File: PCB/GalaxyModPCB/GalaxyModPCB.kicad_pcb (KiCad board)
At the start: 2 copper layers, 63.5 x 38.2 mm, 65 parts, among them J1 LED RGBW Connector, J2 USB to UART, J3 Motor Connector, J4 Projector Connector, J5 Debug Header, J6 Power Header, J7 Boot mode, Q1 IRLML0030, Q2 IRLML0030, Q3 IRLML0030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

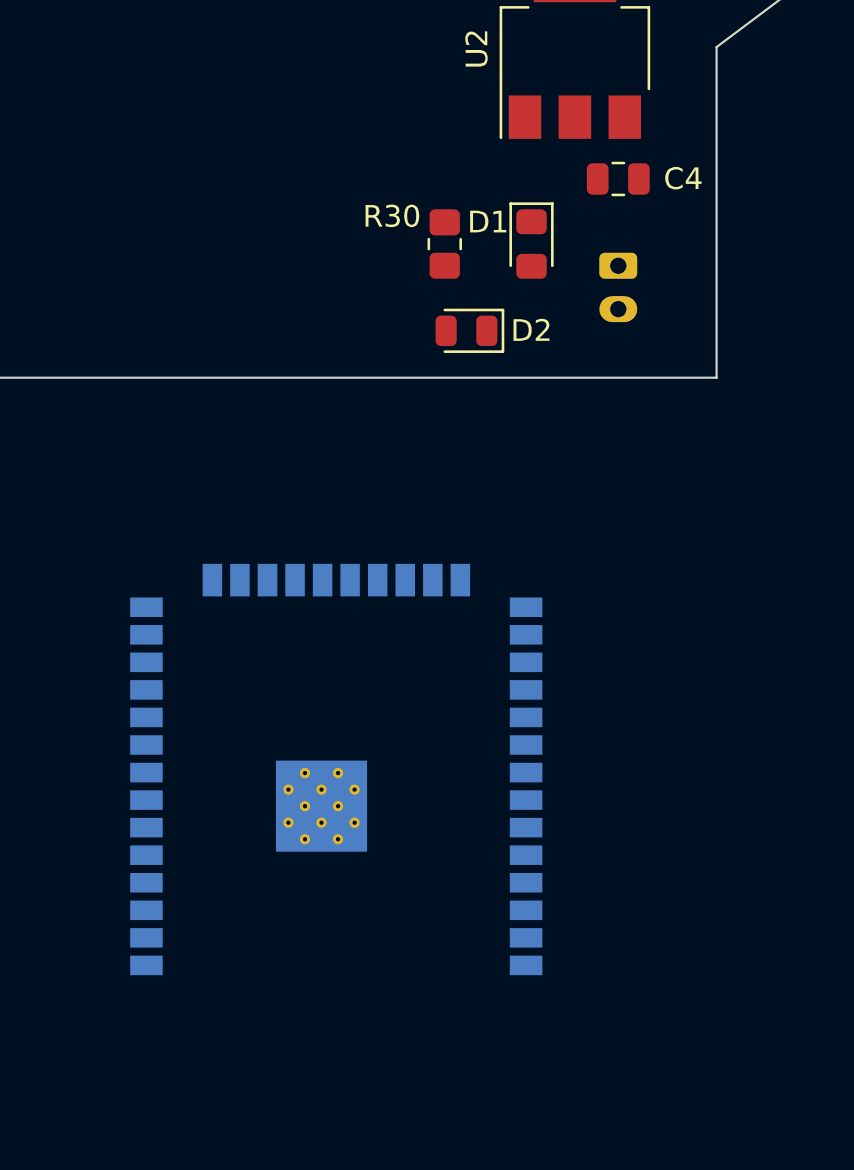
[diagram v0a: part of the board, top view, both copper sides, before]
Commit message: Wired power circuitry
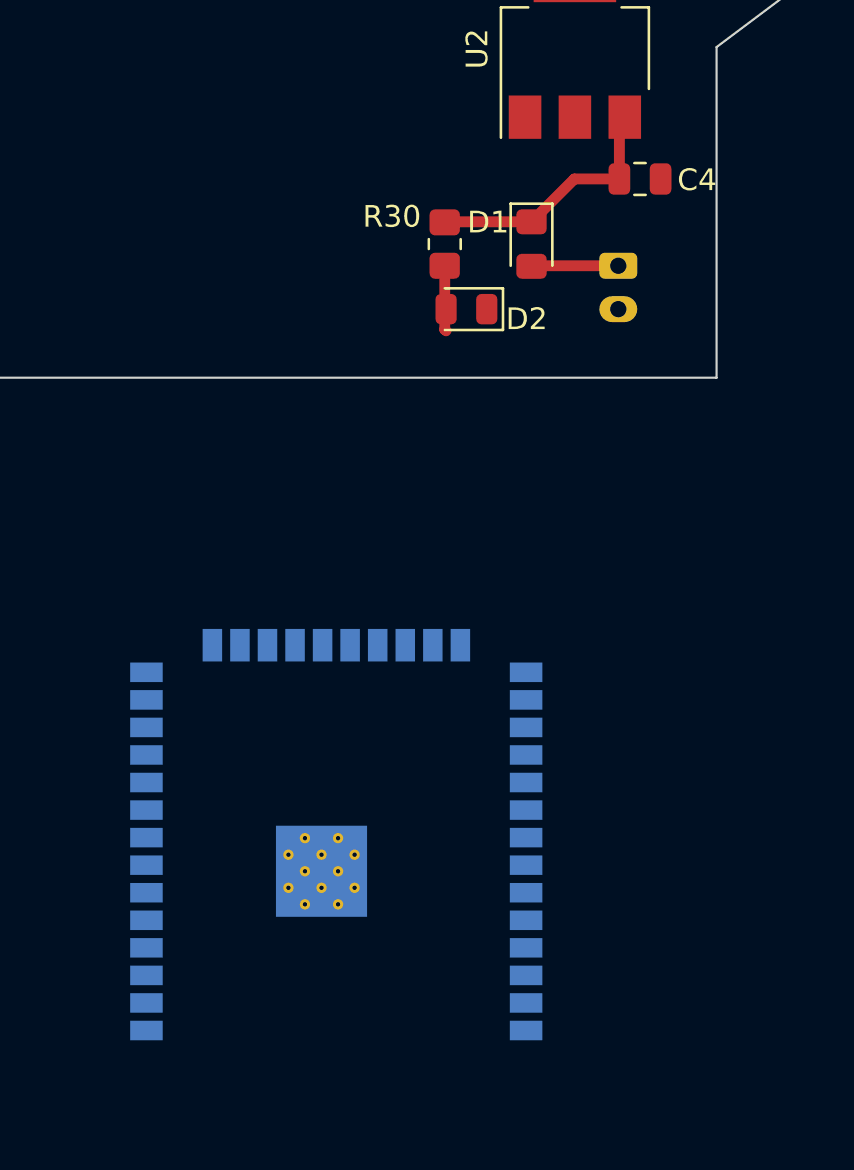
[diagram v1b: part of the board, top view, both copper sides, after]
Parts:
- moved U1 3.00 mm to (142.0, 111.0)
- moved C4 1.00 mm to (156.0, 80.0)
- moved D2 1.00 mm to (148.0, 86.0)
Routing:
- net Net-(C4-Pad1): track 0.00 -> 10.9 mm
- net Net-(J1-Pad1): track 0.00 -> 4.01 mm
- net Net-(D2-Pad2): track 0.00 -> 3.03 mm
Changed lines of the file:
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@@
   )
   (setup
+    (stackup
+      (layer "F.SilkS" (type "Top Silk Screen"))
+      (layer "F.Paste" (type "Top Solder Paste"))
+      (layer "F.Mask" (type "Top Solder Mask") (thickness 0.01))
+      (layer "F.Cu" (type "copper") (thickness 0.035))
+      (layer "dielectric 1" (type "core") (thickness 1.51) (material "FR4") (epsilon_r 4.5) (loss_tangent 0.02))
+      (layer "B.Cu" (type "copper") (thickness 0.035))
+      (layer "B.Mask" (type "Bottom Solder Mask") (thickness 0.01))
+      (layer "B.Paste" (type "Bottom Solder Paste"))
+      (layer "B.SilkS" (type "Bottom Silk Screen"))
+      (copper_finish "None")
+      (dielectric_constraints no)
+    )
     (pad_to_mask_clearance 0)
     (pcbplotparams
@@
   (net 58 "Net-(J1-Pad1)")
   (footprint "Capacitor_SMD:C_0805_2012Metric" (layer "F.Cu")
-    (at 155 80)
+    (at 156 80)
     (descr "Capacitor SMD 0805 (2012 Metric), square (rectangular) end terminal, IPC_7351 nominal, (Body size source: IPC-SM-782 page 76, https://www.pcb-3d.com/wordpress/wp-content/uploads/ipc-sm-782a_amendment_1_and_2.pdf, https://docs.google.com/spreadsheets/d/1BsfQQcO9C6DZCsRaXUlFlo91Tg2WpOkGARC1WS5S8t0/edit?usp=sharing), generated with kicad-footprint-generator")
     (tags "capacitor")
@@
     (property "Sheetname" "")
     (attr smd)
-    (fp_text reference "C4" (at 3 0) (layer "F.SilkS")
+    (fp_text reference "C4" (at 2.63213 0.048771) (layer "F.SilkS")
       (effects (font (size 1 1) (thickness 0.15)))
     )
@@
   )
   (footprint "LED_SMD:LED_0805_2012Metric" (layer "F.Cu")
-    (at 148 87 180)
+    (at 148 86 180)
     (descr "LED SMD 0805 (2012 Metric), square (rectangular) end terminal, IPC_7351 nominal, (Body size source: https://docs.google.com/spreadsheets/d/1BsfQQcO9C6DZCsRaXUlFlo91Tg2WpOkGARC1WS5S8t0/edit?usp=sharing), generated with kicad-footprint-generator")
     (tags "LED")
@@
     (property "Sheetname" "")
     (attr smd)
-    (fp_text reference "D2" (at -3 0) (layer "F.SilkS")
+    (fp_text reference "D2" (at -2.777023 -0.455966) (layer "F.SilkS")
       (effects (font (size 1 1) (thickness 0.15)))
     )
@@
   )
   (footprint "RF_Module:ESP32-WROOM-32" (layer "B.Cu")
-    (at 142 108)
+    (at 142 111)
     (descr "Single 2.4 GHz Wi-Fi and Bluetooth combo chip https://www.espressif.com/sites/default/files/documentation/esp32-wroom-32_datasheet_en.pdf")
     (tags "Single 2.4 GHz Wi-Fi and Bluetooth combo  chip")
@@
       (polygon
         (pts
-          (xy 128 117.97)
-          (xy 156 117.97)
-          (xy 156 128.75)
-          (xy 128 128.75)
+          (xy 128 120.97)
+          (xy 156 120.97)
+          (xy 156 131.75)
+          (xy 128 131.75)
         )
       )
@@
   (gr_line (start 173.5 51.06) (end 173.5 66.3) (layer "Edge.Cuts") (width 0.1))
   (gr_line (start 113.81 71.38) (end 110 71.38) (layer "Edge.Cuts") (width 0.1))
+  (segment (start 155.05 78.05) (end 155 78) (width 0.5) (layer "F.Cu") (net 3))
+  (segment (start 151 81.975) (end 147.025 81.975) (width 0.5) (layer "F.Cu") (net 3))
+  (segment (start 147.025 81.975) (end 147 82) (width 0.5) (layer "F.Cu") (net 3))
+  (segment (start 152.975 80) (end 155.05 80) (width 0.5) (layer "F.Cu") (net 3))
+  (segment (start 155.05 80) (end 155.05 78.05) (width 0.5) (layer "F.Cu") (net 3))
+  (segment (start 151 81.975) (end 152.975 80) (width 0.5) (layer "F.Cu") (net 3))
+  (segment (start 147 84) (end 147 86.9375) (width 0.5) (layer "F.Cu") (net 10))
+  (segment (start 147 86.9375) (end 147.0625 87) (width 0.5) (layer "F.Cu") (net 10))
+  (segment (start 151.025 84) (end 151 84.025) (width 0.5) (layer "F.Cu") (net 58))
+  (segment (start 155 84) (end 151.025 84) (width 0.5) (layer "F.Cu") (net 58))
 )

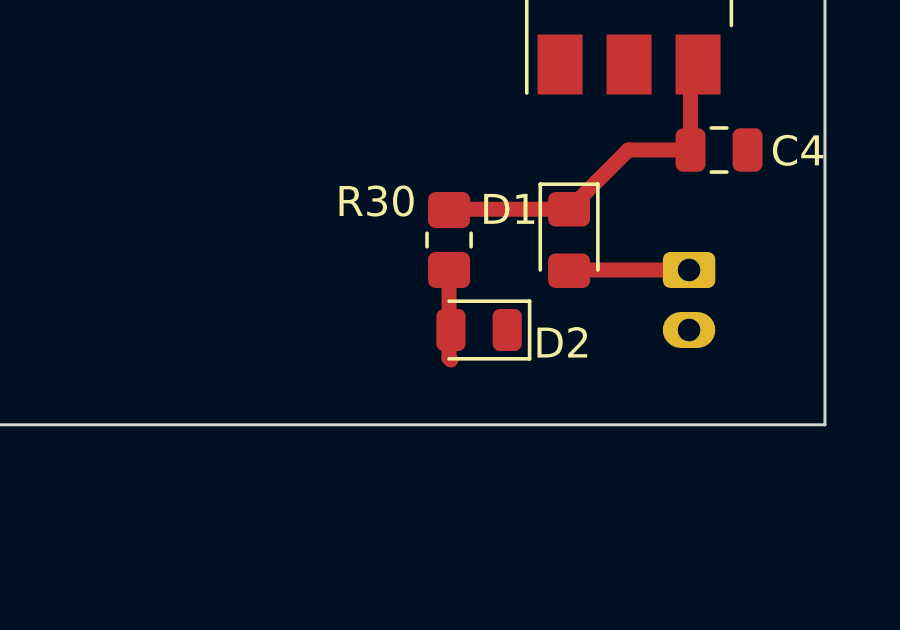
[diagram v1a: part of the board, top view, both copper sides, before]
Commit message: Fixed small tracing issue
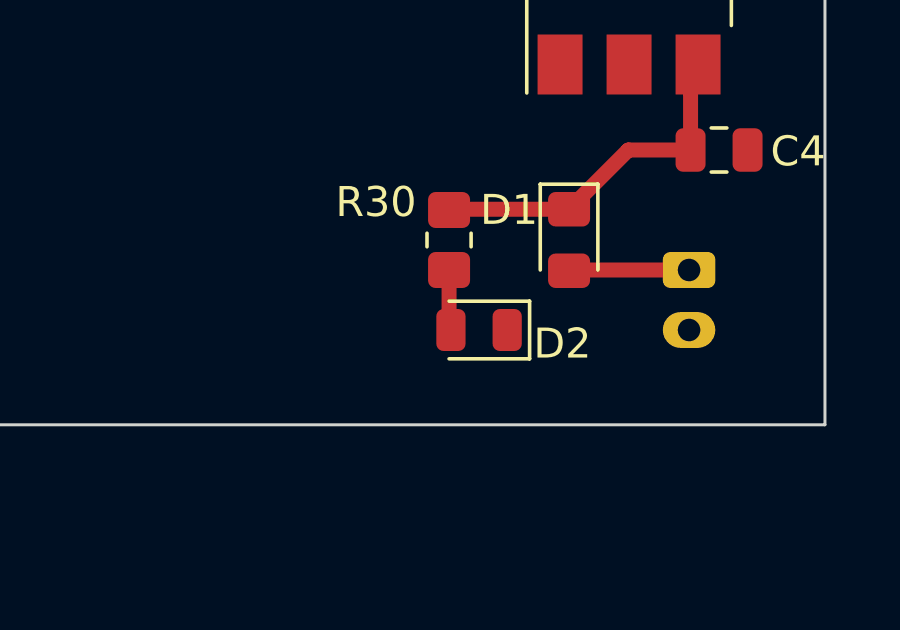
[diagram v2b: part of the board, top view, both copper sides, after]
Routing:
- net Net-(D2-Pad2): track 3.03 -> 2.03 mm
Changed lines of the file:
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@@
   (segment (start 155.05 80) (end 155.05 78.05) (width 0.5) (layer "F.Cu") (net 3))
   (segment (start 151 81.975) (end 152.975 80) (width 0.5) (layer "F.Cu") (net 3))
-  (segment (start 147 84) (end 147 86.9375) (width 0.5) (layer "F.Cu") (net 10))
-  (segment (start 147 86.9375) (end 147.0625 87) (width 0.5) (layer "F.Cu") (net 10))
+  (segment (start 147 85.9375) (end 147.0625 86) (width 0.5) (layer "F.Cu") (net 10))
+  (segment (start 147 84) (end 147 85.9375) (width 0.5) (layer "F.Cu") (net 10))
   (segment (start 151.025 84) (end 151 84.025) (width 0.5) (layer "F.Cu") (net 58))
   (segment (start 155 84) (end 151.025 84) (width 0.5) (layer "F.Cu") (net 58))

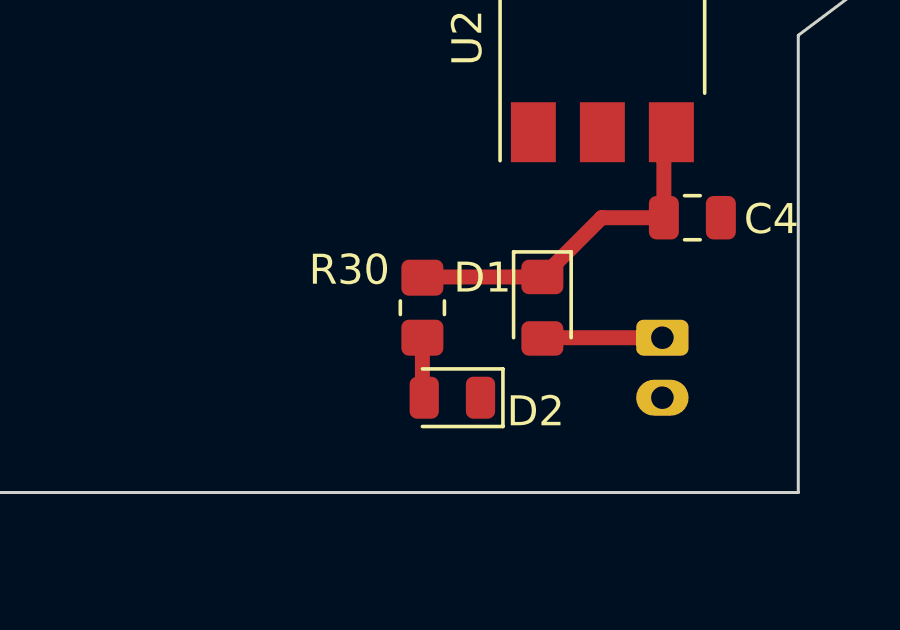
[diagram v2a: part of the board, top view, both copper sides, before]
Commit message: Fixed traces
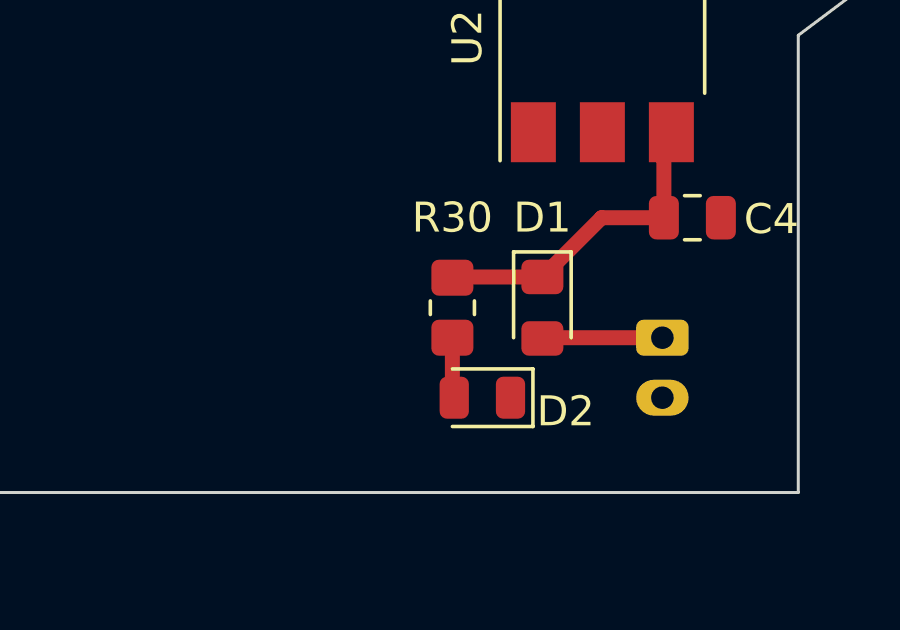
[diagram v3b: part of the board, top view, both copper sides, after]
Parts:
- moved D2 1.00 mm to (149.0, 86.0)
- moved R30 1.00 mm to (148.0, 83.0)
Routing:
- net Net-(C4-Pad1): track 10.9 -> 9.90 mm
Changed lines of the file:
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@@
       (effects (font (size 1 1) (thickness 0.15)))
     )
-    (fp_text value "22uF/10V(20%)" (at -8 0) (layer "F.Fab")
+    (fp_text value "22uF/10V(20%)" (at 12 0) (layer "F.Fab")
       (effects (font (size 1 1) (thickness 0.15)))
     )
@@
   )
   (footprint "Resistor_SMD:R_0805_2012Metric_Pad1.20x1.40mm_HandSolder" (layer "F.Cu")
-    (at 147 83 90)
+    (at 148 83 90)
     (descr "Resistor SMD 0805 (2012 Metric), square (rectangular) end terminal, IPC_7351 nominal with elongated pad for handsoldering. (Body size source: IPC-SM-782 page 72, https://www.pcb-3d.com/wordpress/wp-content/uploads/ipc-sm-782a_amendment_1_and_2.pdf), generated with kicad-footprint-generator")
     (tags "resistor handsolder")
@@
     (property "Sheetname" "")
     (attr smd)
-    (fp_text reference "R30" (at 1.262462 -2.435593 180) (layer "F.SilkS")
+    (fp_text reference "R30" (at 3 0 180) (layer "F.SilkS")
       (effects (font (size 1 1) (thickness 0.15)))
     )
-    (fp_text value "2K(5%)" (at -2 -4 180) (layer "F.Fab")
+    (fp_text value "2K(5%)" (at -3 19 180) (layer "F.Fab")
       (effects (font (size 1 1) (thickness 0.15)))
     )
@@
     (property "Sheetname" "")
     (attr smd)
-    (fp_text reference "D1" (at -1 2 180) (layer "F.SilkS")
+    (fp_text reference "D1" (at -3 0 180) (layer "F.SilkS")
       (effects (font (size 1 1) (thickness 0.15)))
     )
-    (fp_text value "RVP Diode" (at 0 9 180) (layer "F.Fab")
+    (fp_text value "RVP Diode" (at 0 -15 180) (layer "F.Fab")
       (effects (font (size 1 1) (thickness 0.15)))
     )
@@
   )
   (footprint "LED_SMD:LED_0805_2012Metric" (layer "F.Cu")
-    (at 148 86 180)
+    (at 149 86 180)
     (descr "LED SMD 0805 (2012 Metric), square (rectangular) end terminal, IPC_7351 nominal, (Body size source: https://docs.google.com/spreadsheets/d/1BsfQQcO9C6DZCsRaXUlFlo91Tg2WpOkGARC1WS5S8t0/edit?usp=sharing), generated with kicad-footprint-generator")
     (tags "LED")
@@
       (effects (font (size 1 1) (thickness 0.15)))
     )
-    (fp_text value "LED" (at 3 -1) (layer "F.Fab")
+    (fp_text value "LED" (at -2 -2) (layer "F.Fab")
       (effects (font (size 1 1) (thickness 0.15)))
     )
@@
   (gr_line (start 113.81 71.38) (end 110 71.38) (layer "Edge.Cuts") (width 0.1))
   (segment (start 155.05 78.05) (end 155 78) (width 0.5) (layer "F.Cu") (net 3))
-  (segment (start 151 81.975) (end 147.025 81.975) (width 0.5) (layer "F.Cu") (net 3))
-  (segment (start 147.025 81.975) (end 147 82) (width 0.5) (layer "F.Cu") (net 3))
   (segment (start 152.975 80) (end 155.05 80) (width 0.5) (layer "F.Cu") (net 3))
   (segment (start 155.05 80) (end 155.05 78.05) (width 0.5) (layer "F.Cu") (net 3))
+  (segment (start 151 81.975) (end 148.025 81.975) (width 0.5) (layer "F.Cu") (net 3))
   (segment (start 151 81.975) (end 152.975 80) (width 0.5) (layer "F.Cu") (net 3))
-  (segment (start 147 85.9375) (end 147.0625 86) (width 0.5) (layer "F.Cu") (net 10))
-  (segment (start 147 84) (end 147 85.9375) (width 0.5) (layer "F.Cu") (net 10))
+  (segment (start 148.025 81.975) (end 148 82) (width 0.5) (layer "F.Cu") (net 3))
+  (segment (start 148 85.9375) (end 148.0625 86) (width 0.5) (layer "F.Cu") (net 10))
+  (segment (start 148 84) (end 148 85.9375) (width 0.5) (layer "F.Cu") (net 10))
   (segment (start 151.025 84) (end 151 84.025) (width 0.5) (layer "F.Cu") (net 58))
   (segment (start 155 84) (end 151.025 84) (width 0.5) (layer "F.Cu") (net 58))
